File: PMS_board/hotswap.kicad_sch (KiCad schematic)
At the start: 28 parts, among them Q10 Q_NMOS_GDS, Q11 Q_NMOS_GDS, Q7 Q_NMOS_GDS, Q8 Q_NMOS_GDS, Q9 Q_NMOS_GDS, U12 LM74800QDRRRQ1, U14 LM74800QDRRRQ1, U18 IRFS7530TRL7PP

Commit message: fix hotswap
hotswap looks better now :)
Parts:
- removed C22: 10nF, Capacitor_SMD:C_0603_1608Metric_Pad1.08x0.95mm_HandSolder, symbol Device:C
- removed C23, C27, C42, C57: 1uF, Capacitor_SMD:C_0603_1608Metric_Pad1.08x0.95mm_HandSolder, symbol Device:C
- removed C43, C56: 47uF, Capacitor_SMD:C_0603_1608Metric_Pad1.08x0.95mm_HandSolder, symbol Device:C_Polarized_US
- removed C44, C55: 0.1uF, Capacitor_SMD:C_0603_1608Metric_Pad1.08x0.95mm_HandSolder, symbol Device:C
- removed D4, D5: PTVS26VZ1USK, Diode_SMD:Nexperia_DSN1608-2_1.6x0.8mm, symbol Diode:PTVS26VZ1USK
- removed Q10, Q11, Q7, Q8: Q_NMOS_GDS, IRFS7530TRL7PP:PG-TO263-7_INF-M, symbol Transistor_FET:Q_NMOS_GDS
- removed Q9: Q_NMOS_GDS, symbol Transistor_FET:Q_NMOS_GDS
- removed R29, R30: 47, Resistor_SMD:R_0603_1608Metric_Pad0.98x0.95mm_HandSolder, symbol Device:R_US
- removed R37, R41: 100k, Resistor_SMD:R_0603_1608Metric_Pad0.98x0.95mm_HandSolder, symbol Device:R_US
- removed R38, R40: 3.48k, Resistor_SMD:R_0603_1608Metric_Pad0.98x0.95mm_HandSolder, symbol Device:R_US
- removed R42: 10k, Resistor_SMD:R_0603_1608Metric_Pad0.98x0.95mm_HandSolder, symbol Device:R_US
- removed U12: LM74800QDRRRQ1, LM74800QDRRRQ1:IC_LM74800QDRRRQ1, symbol LM74800QDRRRQ1:LM74800QDRRRQ1
- removed U18: IRFS7530TRL7PP, PG-TO263-7_INF, symbol IRFS7530TRL7PP:IRFS7530TRL7PP
- added C30, C33: 10nF, Capacitor_SMD:C_0603_1608Metric_Pad1.08x0.95mm_HandSolder, symbol Device:C
- added C31, C32, C62, C64: 1uF, Capacitor_SMD:C_0603_1608Metric_Pad1.08x0.95mm_HandSolder, symbol Device:C
- added C58: 0.1uF, Capacitor_SMD:C_0603_1608Metric_Pad1.08x0.95mm_HandSolder, symbol Device:C
- added C61, C63: 47uF, Capacitor_SMD:C_0603_1608Metric_Pad1.08x0.95mm_HandSolder, symbol Device:C_Polarized_US
- added D11, D13: PTVS26VZ1USK, Diode_SMD:Nexperia_DSN1608-2_1.6x0.8mm, symbol Diode:PTVS26VZ1USK
- added R32, R33: 47, Resistor_SMD:R_0603_1608Metric_Pad0.98x0.95mm_HandSolder, symbol Device:R_US
- added R43: 3.48k, Resistor_SMD:R_0603_1608Metric_Pad0.98x0.95mm_HandSolder, symbol Device:R_US
- added R44, R81: 100k, Resistor_SMD:R_0603_1608Metric_Pad0.98x0.95mm_HandSolder, symbol Device:R_US
- added R80, R92: 10k, Resistor_SMD:R_0603_1608Metric_Pad0.98x0.95mm_HandSolder, symbol Device:R_US
- added U13: LM74800QDRRRQ1, LM74800QDRRRQ1:IC_LM74800QDRRRQ1, symbol LM74800QDRRRQ1:LM74800QDRRRQ1
- added U19, U20, U21, U22: IRFS7530TRL7PP, PG-TO263-7_INF, symbol IRFS7530TRL7PP:IRFS7530TRL7PP
- C60: value 10nF -> 0.1uF
- R91: value 10k -> 3.48k
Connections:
- net BattA: now also R80.2, U19.8 (D); no longer R91.1
- net BattB: now also R92.2, U22.8 (D)
- net GND: now also R91.1, C30.2, C31.2, C32.2, C33.2, C61.2, C62.2, C63.2, C64.2, D11.2 (A), D13.2 (A), R43.1, U13.7 (GND); no longer C60.2
- net ORingOut: now also C61.1, C63.1, U13.12 (C), U20.8 (D), U21.8 (D)
- net vsnsB: now reaches U14.10 (VS), U14.3 (VSNS), U14.6 (EN/UVLO)
- net vsnsB: now also C60.2, C32.1, D13.1 (K), R92.1
- net at U14.5 (OV): now also R91.2, R81.1
- net at U14.4 (SW): now also R81.2
- net at C60.1: now also U14.11 (CAP)
- net HGateB: now reaches U14.8 (HGATE)
- net HGateB: now also R33.1, U22.1 (G)
- net sourceB: now reaches U14.2 (A), U14.9 (OUT)
- net sourceB: now also C64.1, U21.2 (S), U21.3 (S), U21.5 (S), U21.6 (S), U21.7 (S), U22.2 (S), U22.3 (S), U22.5 (S), U22.6 (S), U22.7 (S)
- net DGateB: now reaches U14.1 (DGATE)
- net DGateB: now also U21.1 (G)
- new net: C33.1, R33.2
- new net: C30.1, R32.2
- new net: C58.1, U13.11 (CAP)
- new net: R44.2, U13.4 (SW)
- new net: R43.2, R44.1, U13.5 (OV)
- new net DGateA: U13.1 (DGATE), U20.1 (G)
- new net HGateA: R32.1, U13.8 (HGATE), U19.1 (G)
- new net sourceA: C62.1, U13.2 (A), U13.9 (OUT), U19.2 (S), U19.3 (S), U19.5 (S), U19.6 (S), U19.7 (S), U20.2 (S), U20.3 (S), U20.5 (S), U20.6 (S), U20.7 (S)
- new net vsnsA: C31.1, C58.2, D11.1 (K), R80.1, U13.10 (VS), U13.3 (VSNS), U13.6 (EN/UVLO)
- no-connect marks 6 -> 2
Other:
- note removed: "<-- this really means this ^^^"

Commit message: Fixed references
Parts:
- U4: renamed from U22; footprint PG-TO263-7_INF -> IRFS7530TRL7PP:PG-TO263-7_INF
- U5: renamed from U21; footprint PG-TO263-7_INF -> IRFS7530TRL7PP:PG-TO263-7_INF
- U8: renamed from U20; footprint PG-TO263-7_INF -> IRFS7530TRL7PP:PG-TO263-7_INF
- U9: renamed from U19; footprint PG-TO263-7_INF -> IRFS7530TRL7PP:PG-TO263-7_INF
- renumbered C33 to C1, C30 to C10, C60 to C2, C64 to C3, C32 to C4, C61 to C5, C63 to C6, C31 to C7, C62 to C8, C58 to C9, D13 to D10, R33 to R42, R92 to R43, R81 to R44, R91 to R45, R44 to R46, R43 to R47, R80 to R48, R32 to R49, U14 to U6, U13 to U7

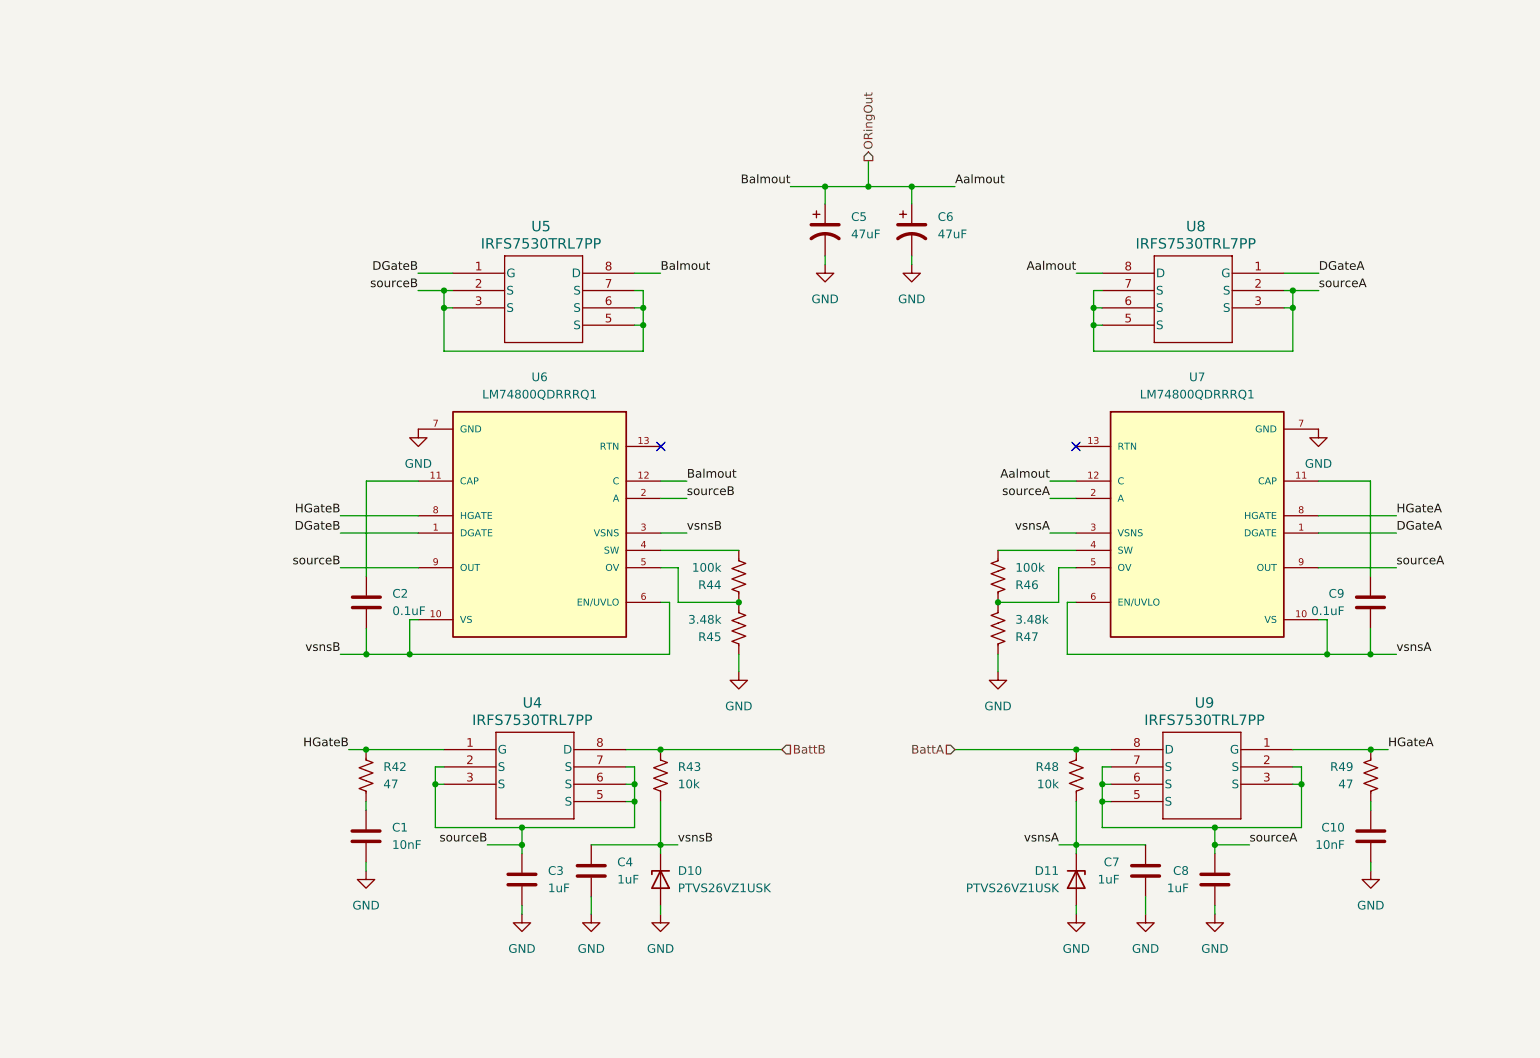
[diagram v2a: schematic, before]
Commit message: Add Fuse, made things look nice
I added fuse symbol, footprint, and datasheet. I organized 2 sheets and condensed schematics
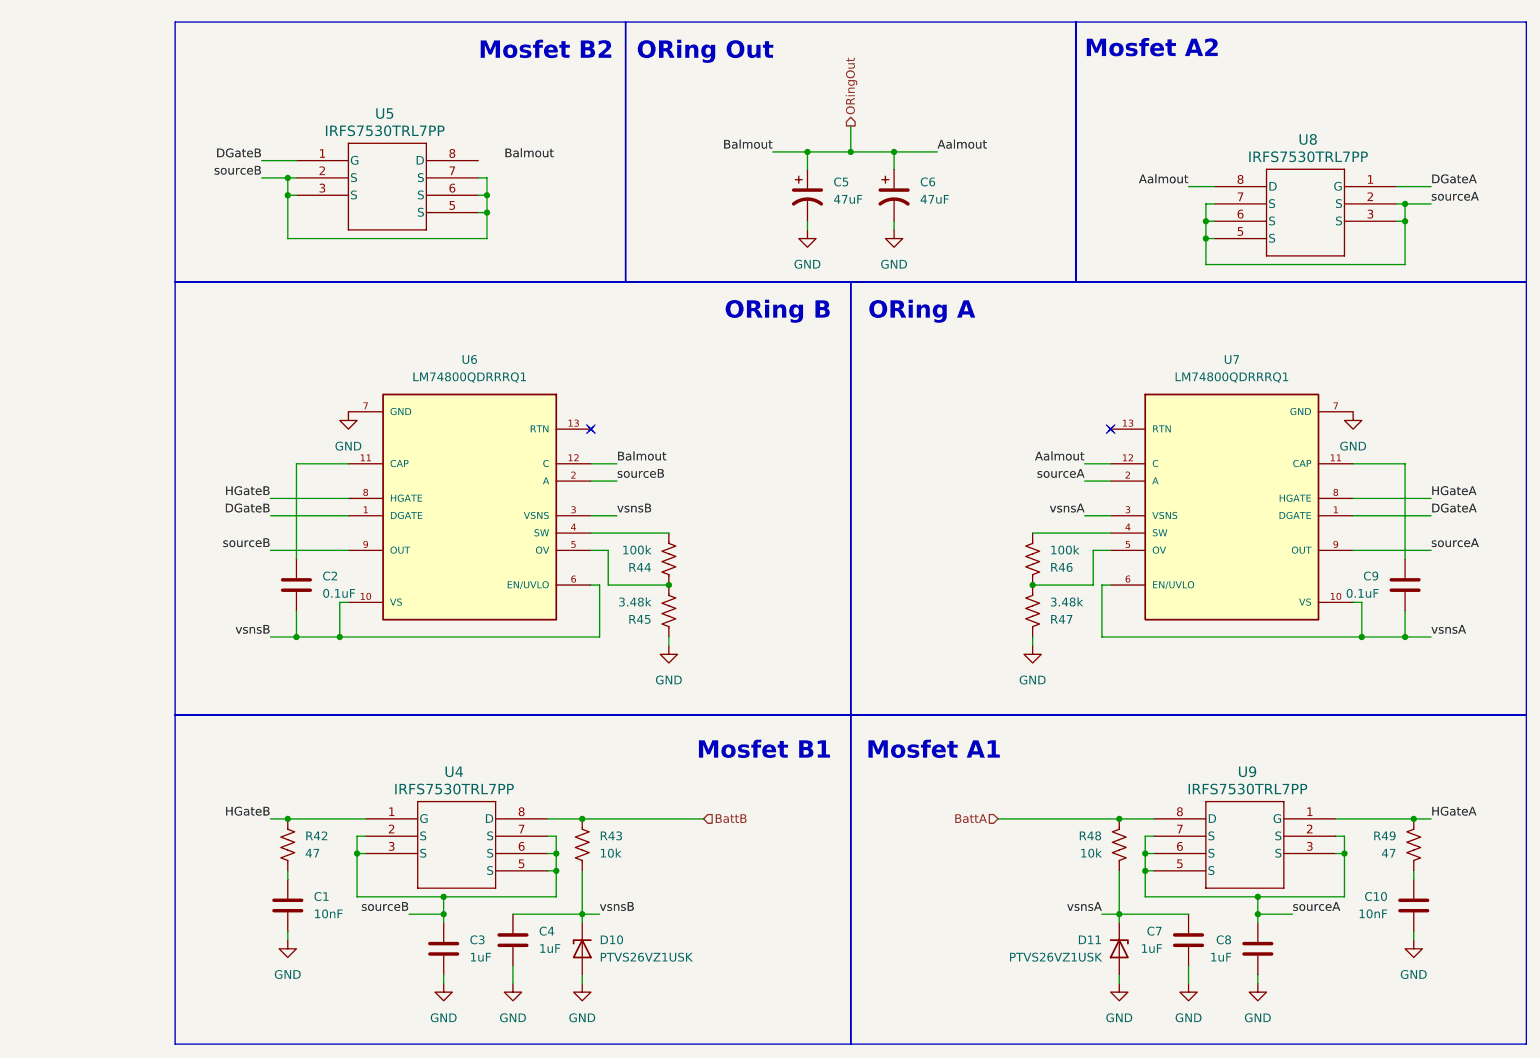
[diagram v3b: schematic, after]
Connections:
- net ORingOut: no longer U5.8 (D)
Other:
- note added: "Mosfet A1"
- note added: "Mosfet A2"
- note added: "Mosfet B1"
- note added: "Mosfet B2"
- note added: "ORing A"
- note added: "ORing B"
- note added: "ORing Out"
- moved on the sheet: C1, C10, C2, C3, C4, C5, C6, C7, C8, C9, D10, D11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

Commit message: Add pins to STM Chip
I also changed chips for jetson and motor out.
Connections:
- net ORingOut: now also U5.8 (D)
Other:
- moved on the sheet: U8
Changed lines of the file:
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@@
 	)
 	(junction
-		(at 226.06 41.91)
+		(at 226.06 38.1)
 		(diameter 0)
 		(color 0 0 0 0)
@@
 	)
 	(junction
-		(at 196.85 46.99)
+		(at 196.85 43.18)
 		(diameter 0)
 		(color 0 0 0 0)
@@
 	)
 	(junction
-		(at 196.85 44.45)
+		(at 196.85 40.64)
 		(diameter 0)
 		(color 0 0 0 0)
@@
 	)
 	(junction
-		(at 226.06 44.45)
+		(at 226.06 40.64)
 		(diameter 0)
 		(color 0 0 0 0)
@@
 	(wire
 		(pts
-			(xy 196.85 46.99) (xy 196.85 50.8)
+			(xy 196.85 43.18) (xy 196.85 46.99)
 		)
 		(stroke
@@
 	(wire
 		(pts
-			(xy 196.85 44.45) (xy 198.12 44.45)
+			(xy 196.85 40.64) (xy 198.12 40.64)
 		)
 		(stroke
@@
 	(wire
 		(pts
-			(xy 229.87 41.91) (xy 226.06 41.91)
+			(xy 229.87 38.1) (xy 226.06 38.1)
 		)
 		(stroke
@@
 	(wire
 		(pts
-			(xy 229.87 39.37) (xy 224.79 39.37)
+			(xy 229.87 35.56) (xy 224.79 35.56)
 		)
 		(stroke
@@
 	(wire
 		(pts
-			(xy 226.06 44.45) (xy 224.79 44.45)
+			(xy 226.06 40.64) (xy 224.79 40.64)
 		)
 		(stroke
@@
 	(wire
 		(pts
-			(xy 196.85 41.91) (xy 198.12 41.91)
+			(xy 196.85 38.1) (xy 198.12 38.1)
 		)
 		(stroke
@@
 	(wire
 		(pts
-			(xy 198.12 39.37) (xy 194.31 39.37)
+			(xy 198.12 35.56) (xy 194.31 35.56)
 		)
 		(stroke
@@
 	(wire
 		(pts
-			(xy 224.79 41.91) (xy 226.06 41.91)
+			(xy 224.79 38.1) (xy 226.06 38.1)
 		)
 		(stroke
@@
 	(wire
 		(pts
-			(xy 226.06 41.91) (xy 226.06 44.45)
+			(xy 226.06 38.1) (xy 226.06 40.64)
 		)
 		(stroke
@@
 	(wire
 		(pts
-			(xy 226.06 44.45) (xy 226.06 50.8)
+			(xy 226.06 40.64) (xy 226.06 46.99)
 		)
 		(stroke
@@
 	(wire
 		(pts
-			(xy 226.06 50.8) (xy 196.85 50.8)
+			(xy 226.06 46.99) (xy 196.85 46.99)
 		)
 		(stroke
@@
 	(wire
 		(pts
-			(xy 196.85 41.91) (xy 196.85 44.45)
+			(xy 196.85 38.1) (xy 196.85 40.64)
 		)
 		(stroke
@@
 	(wire
 		(pts
-			(xy 196.85 44.45) (xy 196.85 46.99)
+			(xy 196.85 40.64) (xy 196.85 43.18)
 		)
 		(stroke
@@
 	(wire
 		(pts
+			(xy 90.17 35.56) (xy 93.98 35.56)
+		)
+		(stroke
+			(width 0)
+			(type default)
+		)
+	)
+	(wire
+		(pts
 			(xy 63.5 38.1) (xy 62.23 38.1)
 		)
@@
 	(wire
 		(pts
-			(xy 196.85 46.99) (xy 198.12 46.99)
+			(xy 196.85 43.18) (xy 198.12 43.18)
 		)
 		(stroke
@@
 	)
 	(label "Aalmout"
-		(at 194.31 39.37 180)
+		(at 194.31 35.56 180)
 		(effects
 			(font
@@
 	)
 	(label "DGateA"
-		(at 229.87 39.37 0)
+		(at 229.87 35.56 0)
 		(effects
 			(font
@@
 	)
 	(label "sourceA"
-		(at 229.87 41.91 0)
+		(at 229.87 38.1 0)
 		(effects
 			(font
@@
 		(lib_name "IRFS7530TRL7PP_1")
 		(lib_id "IRFS7530TRL7PP:IRFS7530TRL7PP")
-		(at 224.79 39.37 0)
+		(at 224.79 35.56 0)
 		(mirror y)
 		(unit 1)
@@
 		(fields_autoplaced yes)
 		(property "Reference" "U8"
-			(at 211.836 32.512 0)
+			(at 211.836 28.702 0)
 			(show_name no)
 			(do_not_autoplace no)
@@
 		)
 		(property "Value" "IRFS7530TRL7PP"
-			(at 211.836 35.052 0)
+			(at 211.836 31.242 0)
 			(show_name no)
 			(do_not_autoplace no)
@@
 		)
 		(property "Footprint" "IRFS7530TRL7PP:PG-TO263-7_INF"
-			(at 224.79 39.37 0)
+			(at 224.79 35.56 0)
 			(hide yes)
 			(show_name no)
@@
 		)
 		(property "Datasheet" "https://www.infineon.com/dgdl/irfs7530-7ppbf.pdf?fileId=5546d462533600a40153563a9d1e21d8"
-			(at 224.79 39.37 0)
+			(at 224.79 35.56 0)
 			(hide yes)
 			(show_name no)
@@
 		)
 		(property "Description" ""
-			(at 224.79 39.37 0)
+			(at 224.79 35.56 0)
 			(hide yes)
 			(show_name no)
@@
 		)
 		(property "KLC_S3.1" ""
-			(at 224.79 39.37 0)
+			(at 224.79 35.56 0)
 			(hide yes)
 			(show_name no)
@@
 		)
 		(property "KLC_S4.1" ""
-			(at 224.79 39.37 0)
+			(at 224.79 35.56 0)
 			(hide yes)
 			(show_name no)
@@
 		)
 		(property "KLC_S6.2" ""
-			(at 224.79 39.37 0)
+			(at 224.79 35.56 0)
 			(hide yes)
 			(show_name no)
@@
 			"baa9e823-58b3-4c2b-9da1-beb6854b13b0" "be606c08-2f20-4d31-8318-6fe4b2b9094e"
 			"bf74275c-21db-4262-9881-8869a7dac631" "c6d59676-b181-4e97-bc8c-3d130e09d3e4"
-			"ed5ecb42-bdb9-4aa0-a131-4632deea2226" "f2b5ca4d-0794-4837-8783-9b419a3c7ed3"
-			"f2dde4b8-260e-46c6-bf9b-9882ae54f4ac"
+			"ed5ecb42-bdb9-4aa0-a131-4632deea2226" "f21dbff7-384d-44ad-a332-37bcfe546fa4"
+			"f2b5ca4d-0794-4837-8783-9b419a3c7ed3" "f2dde4b8-260e-46c6-bf9b-9882ae54f4ac"
 		)
 	)

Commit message: Add Zener
Added zener diode data and footprints.
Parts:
- D10, D11: value PTVS26VZ1USK -> BZX84C15LT1G; footprint Diode_SMD:Nexperia_DSN1608-2_1.6x0.8mm -> BZX84C15LT1G:SOT95P240X111-3N
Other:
- moved on the sheet: D11
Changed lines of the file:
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@@
 	(symbol
 		(lib_id "Diode:PTVS26VZ1USK")
-		(at 184.15 151.13 270)
+		(at 184.15 151.13 90)
+		(mirror x)
 		(unit 1)
 		(body_style 1)
@@
 		(in_pos_files yes)
 		(dnp no)
-		(fields_autoplaced yes)
 		(property "Reference" "D11"
 			(at 181.61 149.8599 90)
@@
 					(size 1.27 1.27)
 				)
-				(justify right)
-			)
-		)
-		(property "Value" "PTVS26VZ1USK"
+				(justify left)
+			)
+		)
+		(property "Value" "BZX84C15LT1G"
 			(at 181.61 152.3999 90)
 			(show_name no)
@@
 					(size 1.27 1.27)
 				)
-				(justify right)
-			)
-		)
-		(property "Footprint" "Diode_SMD:Nexperia_DSN1608-2_1.6x0.8mm"
-			(at 179.705 151.13 0)
-			(hide yes)
-			(show_name no)
-			(do_not_autoplace no)
-			(effects
-				(font
-					(size 1.27 1.27)
-				)
-			)
-		)
-		(property "Datasheet" "https://assets.nexperia.com/documents/data-sheet/PTVS26VZ1USK.pdf"
+				(justify left)
+			)
+		)
+		(property "Footprint" "BZX84C15LT1G:SOT95P240X111-3N"
+			(at 188.595 151.13 0)
+			(hide yes)
+			(show_name no)
+			(do_not_autoplace no)
+			(effects
+				(font
+					(size 1.27 1.27)
+				)
+			)
+		)
+		(property "Datasheet" "https://www.digikey.com/en/products/detail/onsemi/BZX84C15LT1G/918390"
 			(at 184.15 151.13 0)
 			(hide yes)
@@
 			)
 		)
-		(property "Description" "26V, 1850W TVS unidirectional diode, DSN1608-2"
+		(property "Description" "Zener Diode 15 V 250 mW ±6% Surface Mount SOT-23-3"
 			(at 184.15 151.13 0)
 			(hide yes)
@@
 			)
 		)
-		(property "Value" "PTVS26VZ1USK"
+		(property "Value" "BZX84C15LT1G"
 			(at 107.95 152.3999 90)
 			(show_name no)
@@
 			)
 		)
-		(property "Footprint" "Diode_SMD:Nexperia_DSN1608-2_1.6x0.8mm"
+		(property "Footprint" "BZX84C15LT1G:SOT95P240X111-3N"
 			(at 109.855 151.13 0)
 			(hide yes)
@@
 			)
 		)
-		(property "Datasheet" "https://assets.nexperia.com/documents/data-sheet/PTVS26VZ1USK.pdf"
+		(property "Datasheet" "https://www.digikey.com/en/products/detail/onsemi/BZX84C15LT1G/918390"
 			(at 105.41 151.13 0)
 			(hide yes)
@@
 			)
 		)
-		(property "Description" "26V, 1850W TVS unidirectional diode, DSN1608-2"
+		(property "Description" "Zener Diode 15 V 250 mW ±6% Surface Mount SOT-23-3"
 			(at 105.41 151.13 0)
 			(hide yes)

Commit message: Fix Zener diodes
current diode was speced with too low of a breakdown voltage. this has been fixed
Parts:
- D10, D11: value BZX84C15LT1G -> MMSZ5264BT1G; footprint BZX84C15LT1G:SOT95P240X111-3N -> Diode_SMD:D_SOD-123
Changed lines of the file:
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@@
 			)
 		)
-		(property "Value" "BZX84C15LT1G"
+		(property "Value" "MMSZ5264BT1G"
 			(at 181.61 152.3999 90)
 			(show_name no)
@@
 			)
 		)
-		(property "Footprint" "BZX84C15LT1G:SOT95P240X111-3N"
+		(property "Footprint" "Diode_SMD:D_SOD-123"
 			(at 188.595 151.13 0)
 			(hide yes)
@@
 			)
 		)
-		(property "Datasheet" "https://www.digikey.com/en/products/detail/onsemi/BZX84C15LT1G/918390"
+		(property "Datasheet" "https://www.onsemi.com/pdf/datasheet/mmsz5221bt1-d.pdf"
 			(at 184.15 151.13 0)
 			(hide yes)
@@
 			)
 		)
-		(property "Description" "Zener Diode 15 V 250 mW ±6% Surface Mount SOT-23-3"
+		(property "Description" "Zener Diode 60 V 500 mW ±5% Surface Mount SOD-123"
 			(at 184.15 151.13 0)
-			(hide yes)
-			(show_name no)
-			(do_not_autoplace no)
-			(effects
-				(font
-					(size 1.27 1.27)
-				)
-			)
-		)
-		(property "KLC_S3.1" ""
-			(at 184.15 151.13 90)
-			(hide yes)
-			(show_name no)
-			(do_not_autoplace no)
-			(effects
-				(font
-					(size 1.27 1.27)
-				)
-			)
-		)
-		(property "KLC_S4.1" ""
-			(at 184.15 151.13 90)
-			(hide yes)
-			(show_name no)
-			(do_not_autoplace no)
-			(effects
-				(font
-					(size 1.27 1.27)
-				)
-			)
-		)
-		(property "KLC_S6.2" ""
-			(at 184.15 151.13 90)
 			(hide yes)
 			(show_name no)
@@
 			)
 		)
-		(property "Value" "BZX84C15LT1G"
+		(property "Value" "MMSZ5264BT1G"
 			(at 107.95 152.3999 90)
 			(show_name no)
@@
 			)
 		)
-		(property "Footprint" "BZX84C15LT1G:SOT95P240X111-3N"
+		(property "Footprint" "Diode_SMD:D_SOD-123"
 			(at 109.855 151.13 0)
 			(hide yes)
@@
 			)
 		)
-		(property "Datasheet" "https://www.digikey.com/en/products/detail/onsemi/BZX84C15LT1G/918390"
+		(property "Datasheet" "https://www.onsemi.com/pdf/datasheet/mmsz5221bt1-d.pdf"
 			(at 105.41 151.13 0)
 			(hide yes)
@@
 			)
 		)
-		(property "Description" "Zener Diode 15 V 250 mW ±6% Surface Mount SOT-23-3"
+		(property "Description" "Zener Diode 60 V 500 mW ±5% Surface Mount SOD-123"
 			(at 105.41 151.13 0)
 			(hide yes)
 			(show_name no)
-			(do_not_autoplace no)
-			(effects
-				(font
-					(size 1.27 1.27)
-				)
-			)
-		)
-		(property "KLC_S3.1" ""
-			(at 105.41 151.13 90)
-			(hide yes)
-			(show_name no)
-			(do_not_autoplace no)
-			(effects
-				(font
-					(size 1.27 1.27)
-				)
-			)
-		)
-		(property "KLC_S4.1" ""
-			(at 105.41 151.13 90)
-			(hide yes)
-			(show_name no)
-			(do_not_autoplace no)
-			(effects
-				(font
-					(size 1.27 1.27)
-				)
-			)
-		)
-		(property "KLC_S6.2" ""
-			(at 105.41 151.13 90)
-			(hide yes)
-			(show_name no)

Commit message: Settle E-stop w/ ORing
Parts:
- added R1, R2: 10k, Resistor_SMD:R_0603_1608Metric_Pad0.98x0.95mm_HandSolder, symbol Device:R_US
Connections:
- net GND: now also R1.2, R2.2
- net vsnsA: no longer U7.6 (EN/UVLO)
- net vsnsB: no longer U6.6 (EN/UVLO)
- new net EstopA: R1.1, U7.6 (EN/UVLO)
- new net EstopB: R2.1, U6.6 (EN/UVLO)
